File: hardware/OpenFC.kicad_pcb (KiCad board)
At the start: 6 copper layers, 37.9 x 37.9 mm, 168 parts, among them CN1 SM04B-SRSS-TB, J1 5V, J10 5V, J11 5V, J12 5V, J13 5V, J14 5V, J15 5V, J16 5V, J17 5V, J18 5V, J19 5V, J2 5V, J20 5V, J21 5V, J22 5V, J23 5V, J24 5V, J25 5V, J26 5V, J27 5V, J28 5V, J29 5V, J3 5V, J30 5V, J31 5V, J32 5V, J33 5V, J34 5V, J35 5V, J36 5V, J37 5V, J38 5V, J39 5V, J4 5V, J40 5V, J41 5V, J42 5V, J43 5V, J44 5V, J47 5V, J48 5V, J49 5V, J5 5V, J50 5V, J51 5V, J52 5V, J53 5V, J54 5V, J55 5V, J6 5V, J7 5V, J8 5V, J9 5V, P1 SM08B-SRSS-TB(LF)(SN), Q1 AP1606, Q2 AP1606, U1 TS2306A 240GF MSM 9_C2976675, U10 SN74LVC1G3157DTBR, U11 COS8051SOT, U12 TLV7031DPWR, U13 SM03B-SRSS-TB, U14 SM06B-SRSS-TB(LF)(SN), U15 LP5912-1.8DRVR, U2 RP2354B_C39843328, U3 TI LMR51430YFDDCR, U4 TI LMR51430YFDDCR, U5 TPS2116DRLR, U7 LP5912-3.3DRVR, U8 SM06B-SRSS-TB(LF)(SN), U9 LSM6DSV16XTR, X1 XTM25012000JT00351001

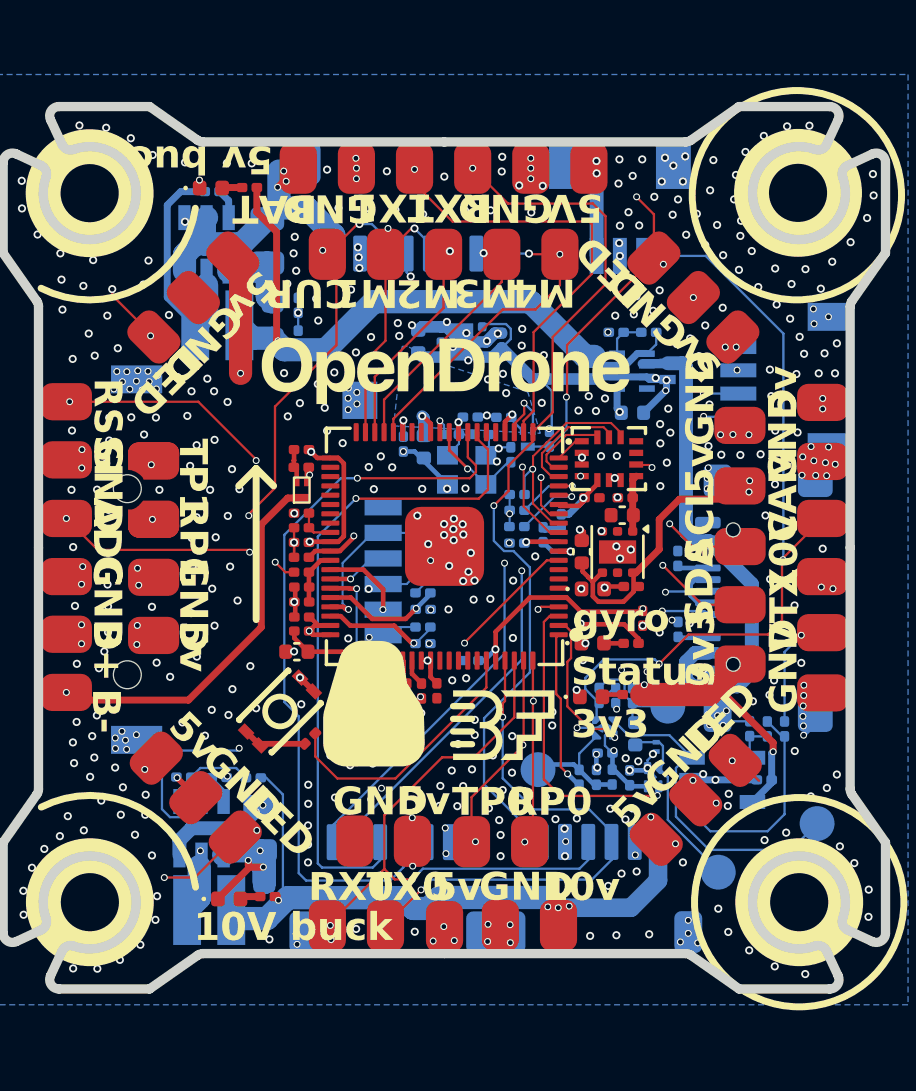
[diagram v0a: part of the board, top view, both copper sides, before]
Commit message: Rev 3: 8S bucks, LP5912 gyro LDO, BMI270, drop the panel project
Power: both bucks are LMR51635YDDCR (U6, U16, C45262770), 4.3-60 V with a 63 V
absolute maximum, replacing the LMR51430YFDDCR whose 38 V absolute maximum left
no margin at 8S. The reference moves from 0.6 V to 0.8 V so the feedback
dividers follow: R22 8.87k for 9.82 V and R24 19.1k for 4.99 V. Same SOT-23-6
land pattern, different pinout, so both buck corners are re-routed.

Gyro supply: U15 LP5912-1.8DRVR placed, along with D9 and R39 which existed in
the Rev 2 schematic but were never placed in the Rev 2 layout. The unused
NCV8187AMT180TAG footprint is gone.

IMU: BMI270 (U9).

Panel: OpenFC_Panel.kicad_pcb and .kicad_pro removed. Production sets come from
OpenFC.kicad_pcb directly now; README updated to match.

ERC and DRC reviewed by the maintainer.

Co-Authored-By: Claude Opus 5 (1M context) <noreply@anthropic.com>
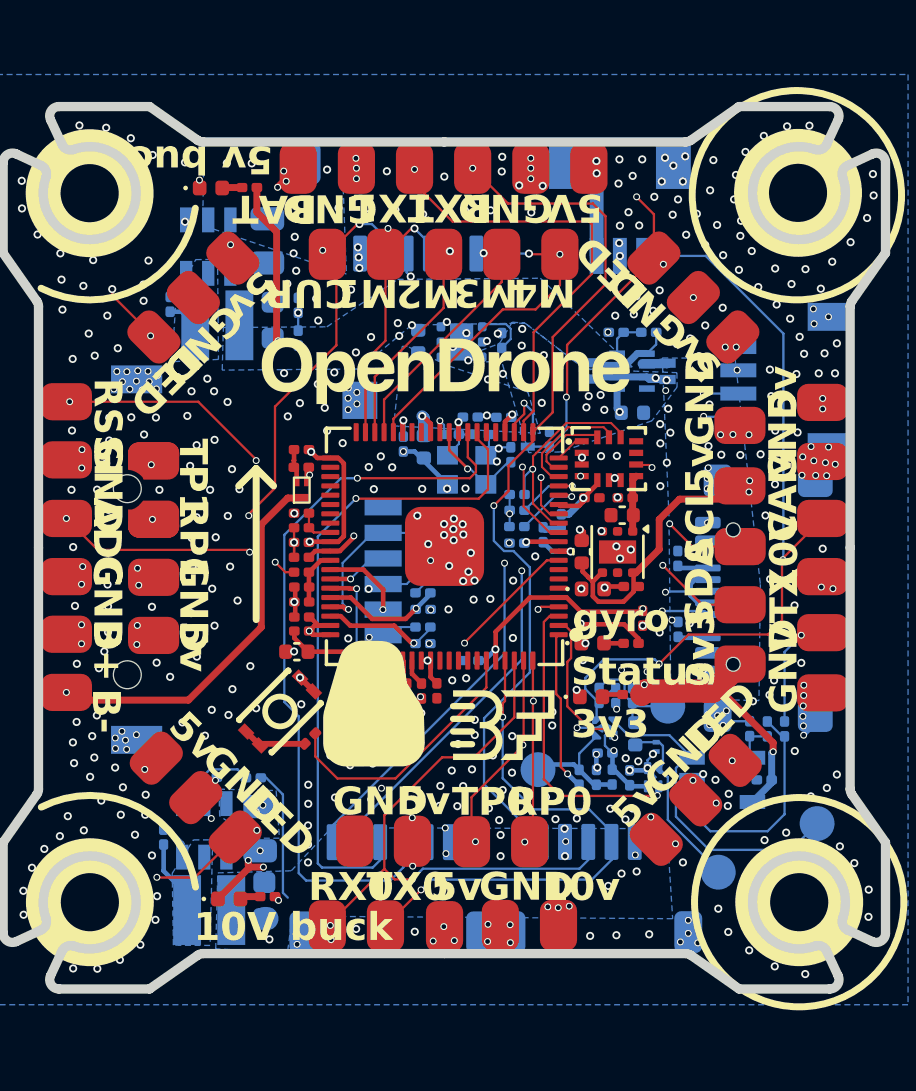
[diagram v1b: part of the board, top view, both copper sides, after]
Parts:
- removed U3, U4: TI LMR51430YFDDCR, lib:SOT-23-6_L2.9-W1.6-P0.95-LS2.9-BL
- added U16: LMR51635YDDCR, lib:SOT-23-6_L2.9-W1.6-P0.95-LS2.8-BL, B.Cu at (142.9, 74.2)
- added U6: LMR51635YDDCR, lib:SOT-23-6_L2.9-W1.6-P0.95-LS2.8-BL, B.Cu at (142.8, 99.3)
- R22: value 6.49k -> 8.87k
- R24: value 13.7k -> 19.1k
- U9: value LSM6DSV16XTR -> BMI270
- moved C25 5.17 mm to (141.3, 76.7), turned to 90 degrees
- moved C24 3.50 mm to (141.0, 99.6), turned to 90 degrees
- moved R22 1.10 mm to (143.0, 97.0), turned to 0 degrees
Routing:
- net +10V: track 54.8 -> 33.3 mm
- net +5V_USB: track 21.7 -> 1.10 mm
- net +5V_BUCK: track 29.3 -> 11.7 mm
- net +BATT: track 49.1 -> 32.6 mm
- net GND: track 99.3 -> 84.1 mm
- net +5V: track 56.4 -> 41.3 mm, vias 27 -> 26
- net Net-(U16-SW): track 9.46 -> 1.32 mm
- net /POWER/10V_ENABLE: track 25.0 -> 21.4 mm
- net Net-(U6-SW): track 6.05 -> 3.24 mm, vias 2 -> 0
- net +3.3V: track 51.4 -> 49.9 mm
- net /PADS/LED_STRIP: track 107.7 -> 106.8 mm
- added copper zone on B.Cu, net +10V
- added copper zone on B.Cu, net +5V
- added copper zone on B.Cu, net +5V_BUCK
- added copper zone on B.Cu, net +5V_USB
- added copper zone on B.Cu, net +BATT
- added copper zone on B.Cu, net Net-(U16-SW)
- added copper zone on B.Cu, net Net-(U6-SW)

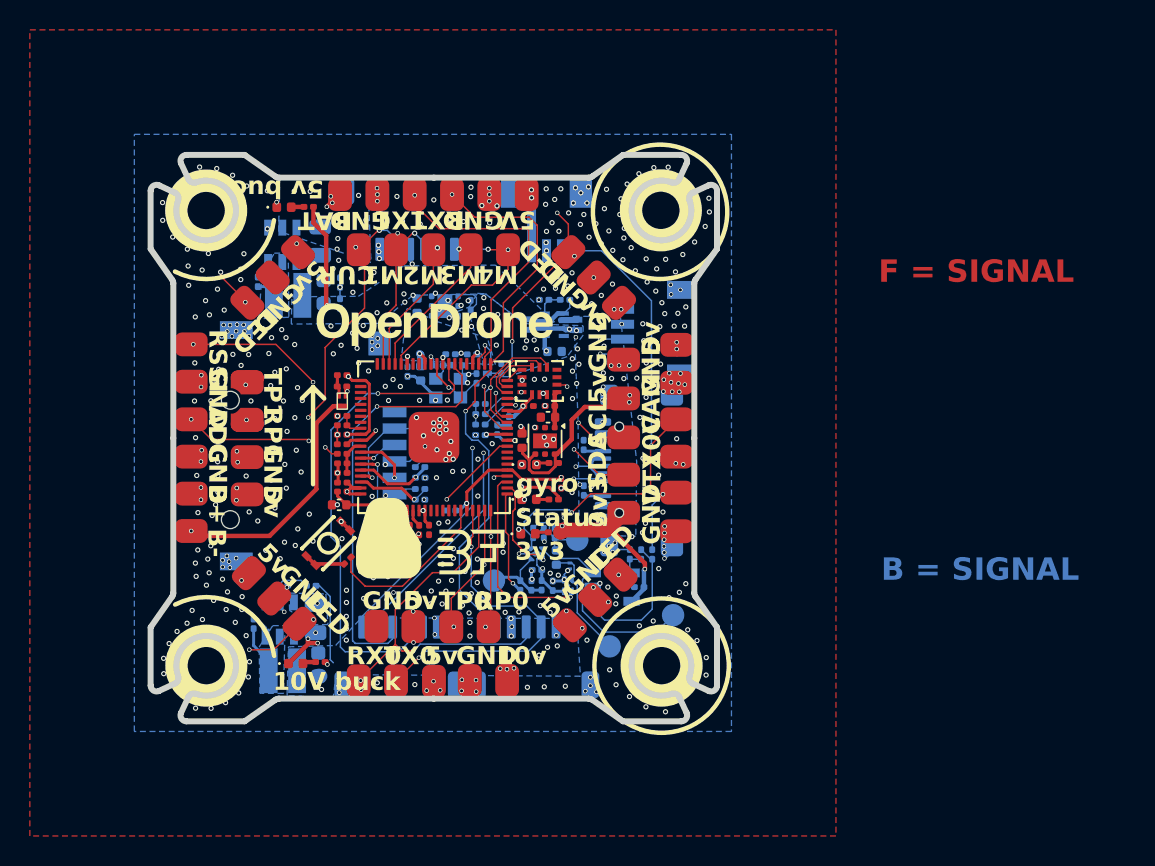
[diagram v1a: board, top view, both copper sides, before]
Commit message: 4V5 rework: TPS2116 mux replaced by DSK24 diode-OR
U5, its RB161QS diodes, R19/R20 and C28 removed. D6 from the buck
output and D10 from +5V_USB feed the new +4v5 net, which supplies the
3.3 V and 1.8 V LDOs, the 6-pin JST and the J5/J47 pads. The buck
output is plain +5V and drives the external 5 V pads directly. All 596
vias at 0.35/0.2, so the line-standard floors pass. DSK24 footprint and
3D model committed with the change. DRC severity choices per Stan.

Co-Authored-By: Claude Opus 5 (1M context) <noreply@anthropic.com>
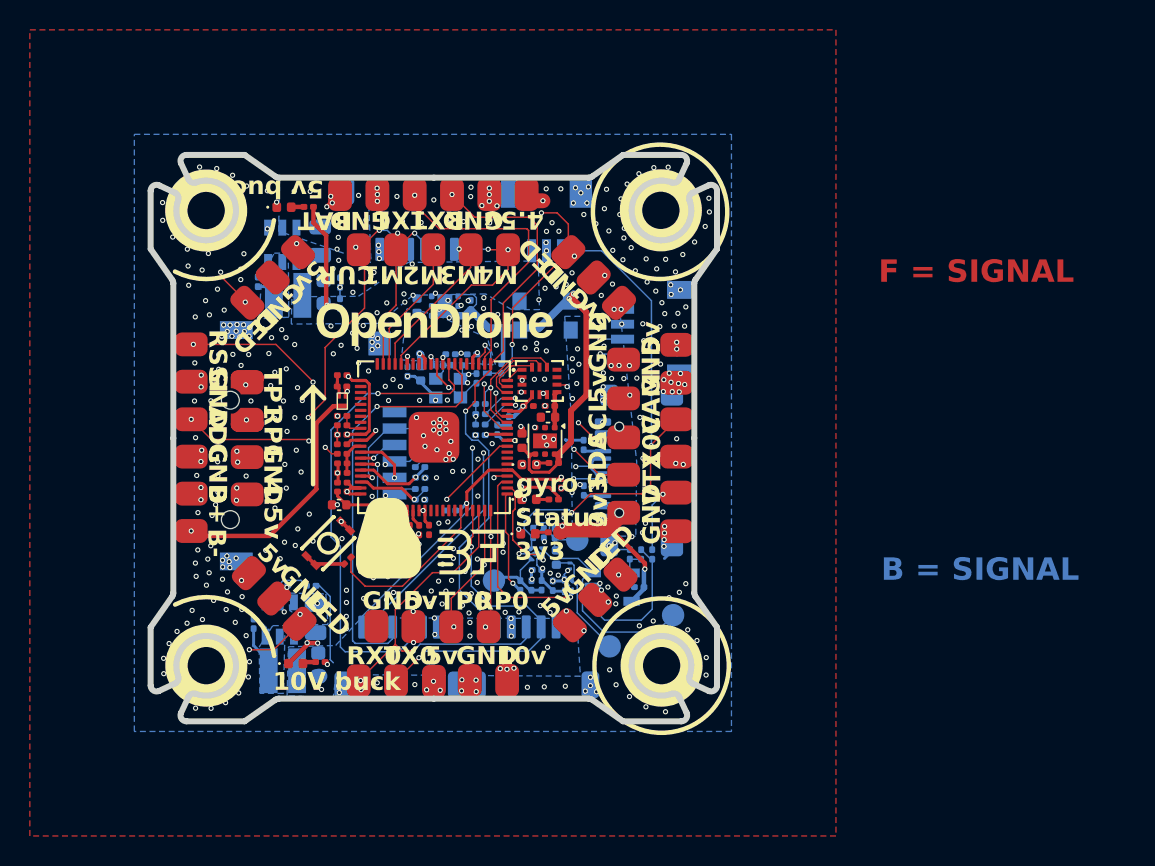
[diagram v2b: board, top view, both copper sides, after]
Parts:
- removed C28: 4.7uF, Capacitor_SMD:C_0402_1005Metric
- removed D2, D3: RB161QS-40_C28646385, lib:SOD-882_L1.0-W0.6-RD
- removed R19: 100k, Resistor_SMD:R_0201_0603Metric
- removed R20: 39k, Resistor_SMD:R_0201_0603Metric
- removed U5: TPS2116DRLR, lib:SOT-583-8_L2.1-W1.6-P0.50-LS1.6-BL
- added D10: DSK24, lib:SOD-123_L2.8-W1.8-LS3.7-RD, B.Cu at (160.6, 79.9)
- added D6: DSK24, lib:SOD-123_L2.8-W1.8-LS3.7-RD, B.Cu at (160.5, 78.0)
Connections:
- C27 pad 1: +5V_BUCK -> +5V
- C30 pad 1: +5V -> +4v5
- C31 pad 1: +5V -> +4v5
- J47 pad 1: +5V -> +4v5
- J5 pad 1: +5V -> +4v5
- L3 pad 2: +5V_BUCK -> +5V
- R18 pad 1: +5V -> +4v5
- R23 pad 2: +5V_BUCK -> +5V
- R26 pad 1: +5V_BUCK -> +5V
- R39 pad 1: +5V -> +4v5
- U14 pad 1: +5V -> +4v5
- U15 pad 4: +5V -> +4v5
- U15 pad 6: +5V -> +4v5
- U7 pad 4: +5V -> +4v5
- U7 pad 6: +5V -> +4v5
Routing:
- net +4v5: track 0.00 -> 110.2 mm, vias 0 -> 7
- net +5V: track 41.3 -> 18.3 mm, vias 26 -> 18
- net +5V_BUCK: track 11.7 -> 0.00 mm, vias 1 -> 0
- net Net-(U5-PR1): track 1.80 -> 0.00 mm
- net +5V_USB: track 1.10 -> 0.00 mm
- net /PADS/LED_STRIP: track 106.8 -> 106.1 mm
- net GND: track 84.1 -> 83.7 mm, vias 482 -> 453
- removed copper zone on B.Cu, net +5V_BUCK
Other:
- board text added: "4.5v"
- board text removed: "5V"

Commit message: Rebuild E6 substitute STEP models from the trusted wrl geometry
The .step files beside these .wrl models were different parts (USB-C
3.5x oversized, etc), and the upstream LCSC .step is the same wrong
file, so kicad-cli --subst-models shipped wrong geometry in every STEP
export while the 3D viewer looked perfect. Rebuilt as tessellated STEP
solids from the .wrl the viewer renders, via
OpenDrone-Scripts/kicad/wrl_to_step.py: bbox and origin now match to
0.000 mm. check_models reports zero E6, export unblocked.

Co-Authored-By: Claude Opus 5 (1M context) <noreply@anthropic.com>
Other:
- board text added: "LN1 = GROUND"
- board text added: "LN3 = PWR"
- board text added: "LN4 = GROUND"
- board text added: "REV3.1"
- board text removed: "LN1 = GROUND (F Reference)"
- board text removed: "LN3 = PWR (5v/3.3v)"
- board text removed: "LN4 = Ground"
